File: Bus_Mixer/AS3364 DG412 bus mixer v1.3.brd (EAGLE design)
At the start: 83.8 x 36.8 mm, 122 parts, among them IC1 PCA9539PW, IC10 DG412-J, IC11 DG412-J, IC2 TL074JT, IC3 TL072JT, IC4 TL074JT, IC5 TL072JT, IC6 TL072JT, IC8 DG412-J, IC9 DG412-J

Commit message: Changed connector values
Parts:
- U$2, U$3: value MA16-1JP -> MA16-1JP-ANGLED
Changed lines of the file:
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@@
 <attribute name="VALUE" x="42.545" y="9.36625" size="1.27" layer="27" rot="R270"/>
 </element>
-<element name="U$2" library="joakim" package="SIP-PIN16-1J" value="MA16-1JP" x="63.5" y="3.01625" smashed="yes">
+<element name="U$2" library="joakim" package="SIP-PIN16-1J" value="MA16-1JP-ANGLED" x="63.5" y="3.01625" smashed="yes">
 <attribute name="VALUE" x="43.18" y="-1.17475" size="1.27" layer="27" ratio="10"/>
 </element>
-<element name="U$3" library="joakim" package="SIP-PIN16-1J" value="MA16-1JP" x="20.32" y="3.01625" smashed="yes">
+<element name="U$3" library="joakim" package="SIP-PIN16-1J" value="MA16-1JP-ANGLED" x="20.32" y="3.01625" smashed="yes">
 <attribute name="VALUE" x="0" y="-1.17475" size="1.27" layer="27" ratio="10"/>
 </element>

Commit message: Updated
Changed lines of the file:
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@@
 <layer number="17" name="Pads" color="2" fill="1" visible="yes" active="yes"/>
 <layer number="18" name="Vias" color="2" fill="1" visible="yes" active="yes"/>
-<layer number="19" name="Unrouted" color="6" fill="1" visible="yes" active="yes"/>
+<layer number="19" name="Unrouted" color="6" fill="1" visible="no" active="yes"/>
 <layer number="20" name="Dimension" color="24" fill="1" visible="yes" active="yes"/>
 <layer number="21" name="tPlace" color="7" fill="1" visible="yes" active="yes"/>
-<layer number="22" name="bPlace" color="7" fill="1" visible="yes" active="yes"/>
+<layer number="22" name="bPlace" color="7" fill="1" visible="no" active="yes"/>
 <layer number="23" name="tOrigins" color="15" fill="1" visible="yes" active="yes"/>
 <layer number="24" name="bOrigins" color="15" fill="1" visible="yes" active="yes"/>
@@
 <layer number="38" name="bTest" color="7" fill="1" visible="no" active="yes"/>
 <layer number="39" name="tKeepout" color="4" fill="11" visible="yes" active="yes"/>
-<layer number="40" name="bKeepout" color="1" fill="11" visible="yes" active="yes"/>
-<layer number="41" name="tRestrict" color="4" fill="10" visible="yes" active="yes"/>
-<layer number="42" name="bRestrict" color="1" fill="10" visible="yes" active="yes"/>
+<layer number="40" name="bKeepout" color="1" fill="11" visible="no" active="yes"/>
+<layer number="41" name="tRestrict" color="4" fill="10" visible="no" active="yes"/>
+<layer number="42" name="bRestrict" color="1" fill="10" visible="no" active="yes"/>
 <layer number="43" name="vRestrict" color="2" fill="10" visible="no" active="yes"/>
 <layer number="44" name="Drills" color="7" fill="1" visible="no" active="yes"/>
@@
 <layer number="50" name="dxf" color="7" fill="1" visible="no" active="no"/>
 <layer number="51" name="tDocu" color="7" fill="1" visible="yes" active="yes"/>
-<layer number="52" name="bDocu" color="7" fill="1" visible="yes" active="yes"/>
+<layer number="52" name="bDocu" color="7" fill="1" visible="no" active="yes"/>
 <layer number="53" name="tGND_GNDA" color="7" fill="9" visible="no" active="no"/>
 <layer number="54" name="bGND_GNDA" color="1" fill="9" visible="no" active="no"/>
@@
 <wire x1="12.54125" y1="25.24125" x2="4.1275" y2="25.24125" width="0.254" layer="1"/>
 <wire x1="4.1275" y1="25.24125" x2="1.11125" y2="22.225" width="0.254" layer="1"/>
-<wire x1="14.07325" y1="21.59" x2="14.0669" y2="21.58365" width="0.254" layer="1"/>
 <contactref element="U$3" pad="1"/>
 <wire x1="14.07325" y1="21.59" x2="12.99845" y2="21.59" width="0.254" layer="1"/>

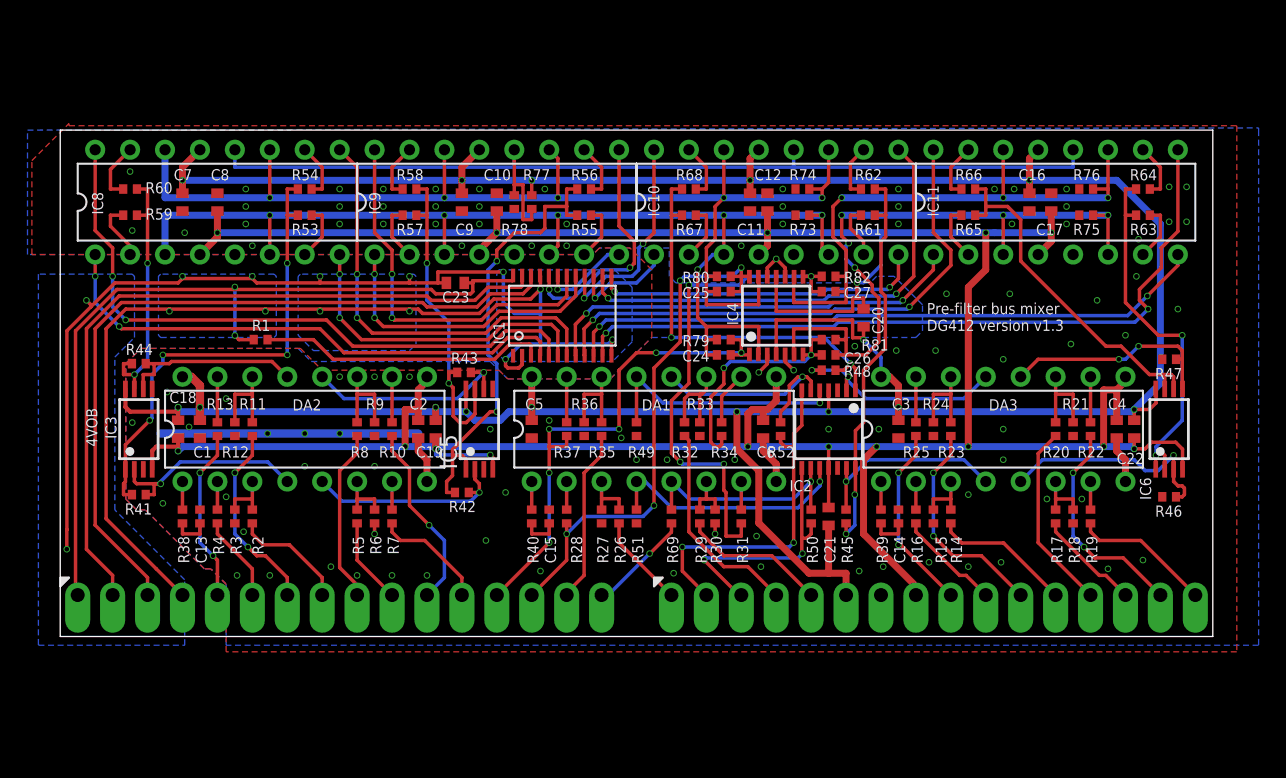
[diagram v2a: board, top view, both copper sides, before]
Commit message: Updated decoupling caps. Tested with JLCPCB
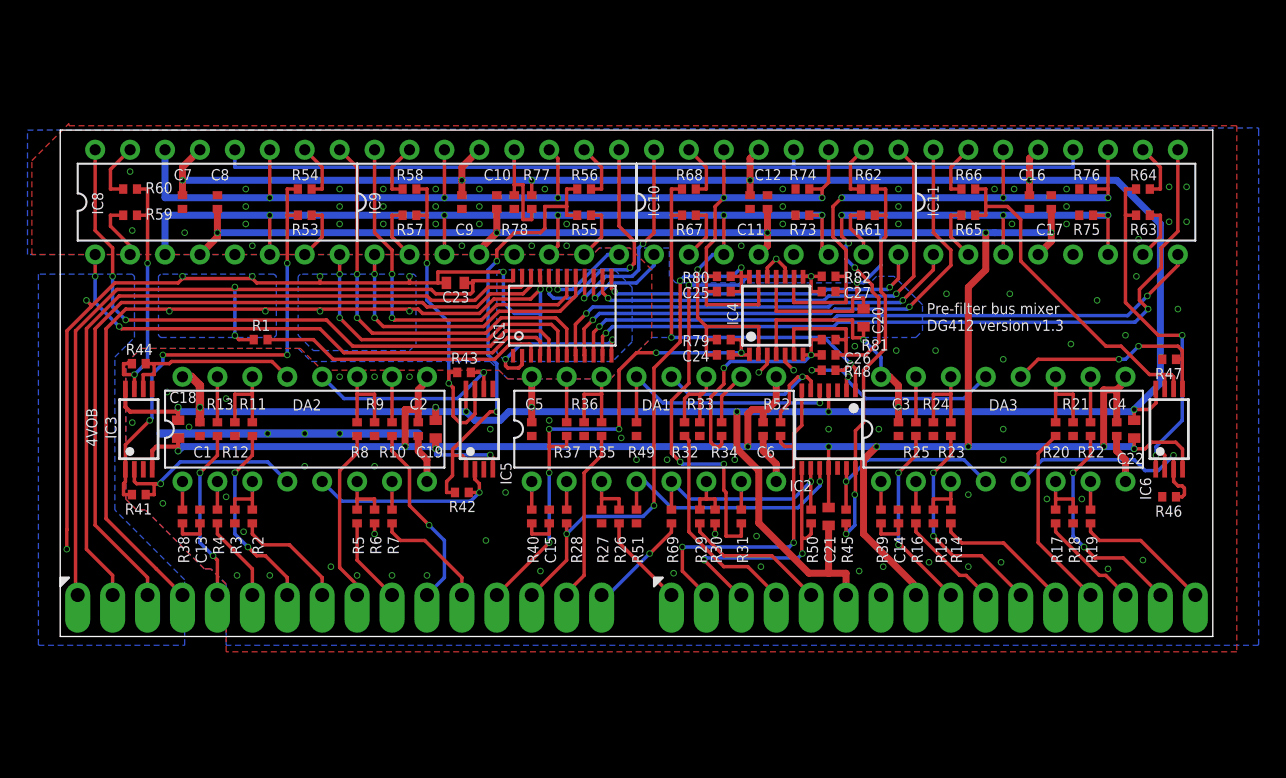
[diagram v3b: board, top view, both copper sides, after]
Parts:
- C1, C10, C11, C12, C16, C17, C2, C3, C4, C5, C6, C7, C8, C9: value 100nF -> 1uF; device rcl:C0402 -> joakim:C0402-J
- C18, C19, C20, C21, C22, C23: value 100nF -> 1uF
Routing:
- net +12V: track 235.0 -> 236.1 mm
- net -12V: track 235.0 -> 236.1 mm

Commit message: Added screw holes
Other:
- board size 83.8 x 36.8 mm -> 83.8 x 42.9 mm
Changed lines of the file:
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@@
 <setting verticaltext="up"/>
 </settings>
-<grid distance="12.5" unitdist="mil" unit="mil" style="lines" multiple="1" display="yes" altdistance="5" altunitdist="mil" altunit="mil"/>
+<grid distance="12.5" unitdist="mil" unit="mm" style="lines" multiple="1" display="yes" altdistance="5" altunitdist="mil" altunit="mil"/>
 <layers>
 <layer number="1" name="Top" color="4" fill="1" visible="yes" active="yes"/>
@@
 <layer number="43" name="vRestrict" color="2" fill="10" visible="no" active="yes"/>
 <layer number="44" name="Drills" color="7" fill="1" visible="no" active="yes"/>
-<layer number="45" name="Holes" color="7" fill="1" visible="no" active="yes"/>
+<layer number="45" name="Holes" color="7" fill="1" visible="yes" active="yes"/>
 <layer number="46" name="Milling" color="3" fill="1" visible="no" active="yes"/>
 <layer number="47" name="Measures" color="7" fill="1" visible="no" active="yes"/>
 <layer number="48" name="Document" color="7" fill="1" visible="no" active="yes"/>
-<layer number="49" name="Reference" color="7" fill="1" visible="no" active="yes"/>
+<layer number="49" name="Reference" color="7" fill="1" visible="yes" active="yes"/>
 <layer number="50" name="dxf" color="7" fill="1" visible="no" active="no"/>
 <layer number="51" name="tDocu" color="7" fill="1" visible="yes" active="yes"/>
@@
 <plain>
 <wire x1="0" y1="0" x2="83.82" y2="0" width="0" layer="20"/>
-<wire x1="83.82" y1="0" x2="83.82" y2="36.83" width="0" layer="20"/>
-<wire x1="83.82" y1="36.83" x2="0" y2="36.83" width="0" layer="20"/>
-<wire x1="0" y1="36.83" x2="0" y2="0" width="0" layer="20"/>
+<wire x1="83.82" y1="0" x2="83.82" y2="42.8625" width="0" layer="20"/>
+<wire x1="83.82" y1="42.8625" x2="79.0575" y2="42.8625" width="0" layer="20"/>
+<wire x1="79.0575" y1="42.8625" x2="73.025" y2="36.83" width="0" layer="20"/>
+<wire x1="73.025" y1="36.83" x2="10.795" y2="36.83" width="0" layer="20"/>
+<wire x1="10.795" y1="36.83" x2="4.7625" y2="42.8625" width="0" layer="20"/>
+<wire x1="4.7625" y1="42.8625" x2="0" y2="42.8625" width="0" layer="20"/>
+<wire x1="0" y1="42.8625" x2="0" y2="0" width="0" layer="20"/>
 <text x="63.02375" y="22.225" size="0.8128" layer="25" font="vector">Pre-filter bus mixer
 DG412 version v1.3</text>
@@
 <text x="31.115" y="4.60375" size="1.27" layer="26" font="vector" rot="MR90">SUM A</text>
 <text x="38.735" y="4.60375" size="1.27" layer="26" font="vector" rot="MR90">CHAIN</text>
+<hole x="2.54" y="39.6875" drill="3.2"/>
+<circle x="2.54" y="39.6875" radius="3" width="0.254" layer="49"/>
+<hole x="81.28" y="39.6875" drill="3.2"/>
+<circle x="81.28" y="39.6875" radius="3" width="0.254" layer="49"/>
 </plain>
 <attributes>

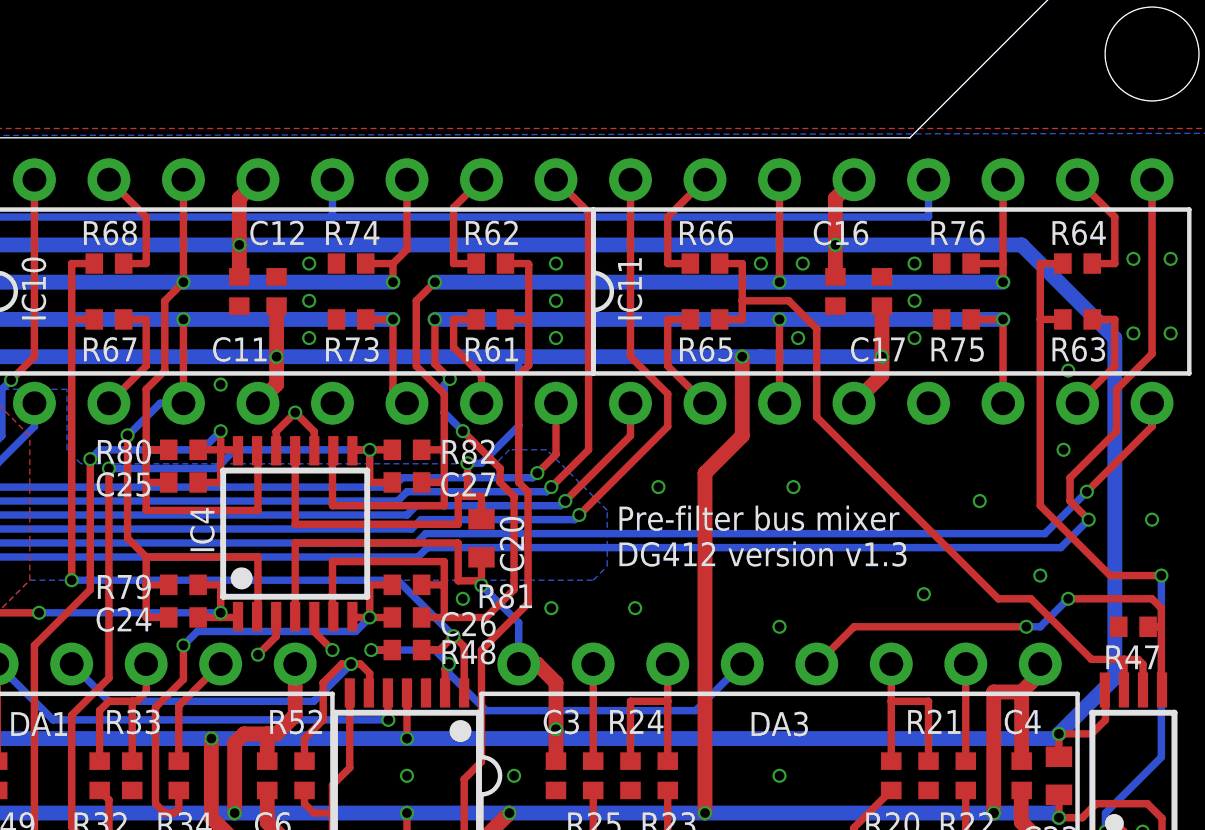
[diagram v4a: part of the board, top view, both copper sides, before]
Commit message: Fixed extended resistor
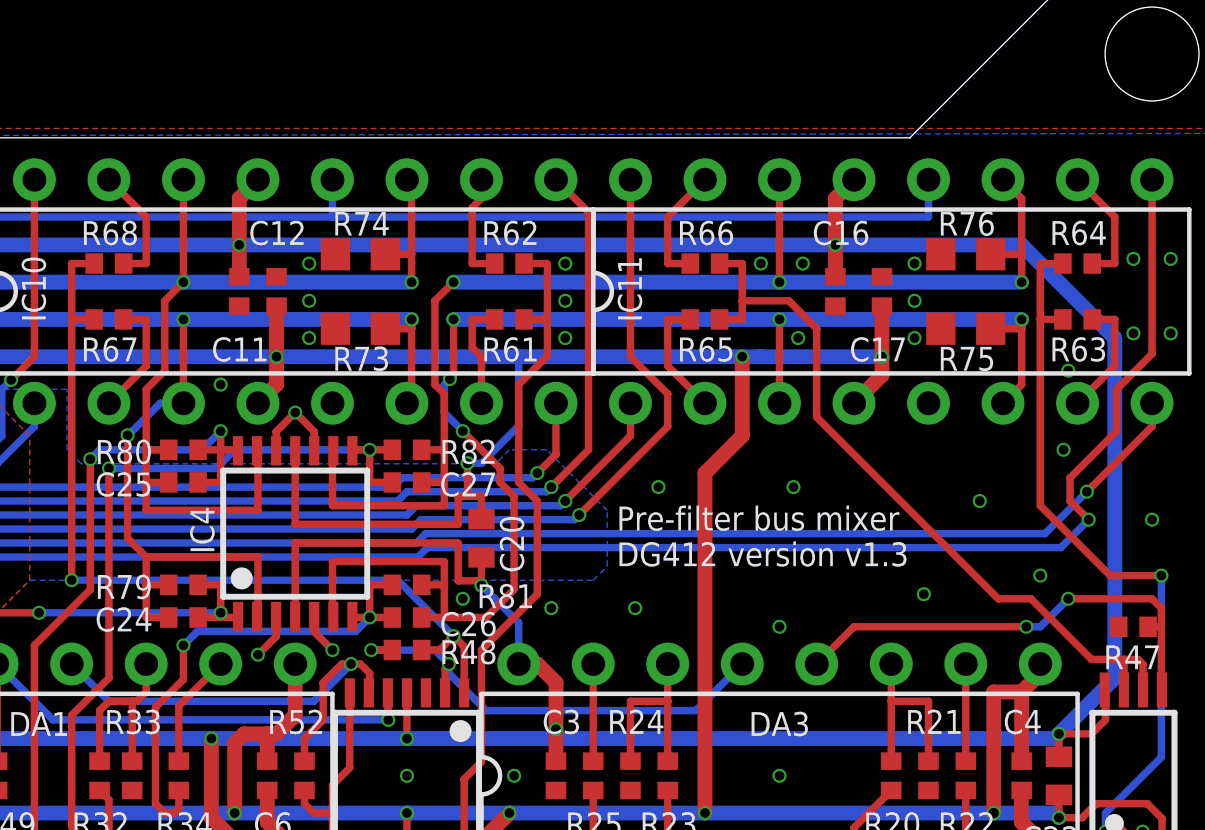
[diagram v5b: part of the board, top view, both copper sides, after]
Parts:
- R73, R74, R75, R76: device rcl:R0402 -> rcl:R0603
- moved R61 0.64 mm to (59.4, 30.6)
- moved R62 0.64 mm to (59.4, 32.5)
- moved R75 0.45 mm to (74.9, 30.3)
- moved R76 0.45 mm to (74.9, 32.9)
- moved R73 0.45 mm to (54.3, 30.3)
- moved R74 0.45 mm to (54.3, 32.9)
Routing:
- net BUS_A: track 82.5 -> 83.3 mm
- net OUT6: track 28.9 -> 29.4 mm
